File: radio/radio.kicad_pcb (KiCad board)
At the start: 2 copper layers, 63.5 x 63.5 mm, 6 parts, among them J1 CAS_stacking, U1 RFM69HCW

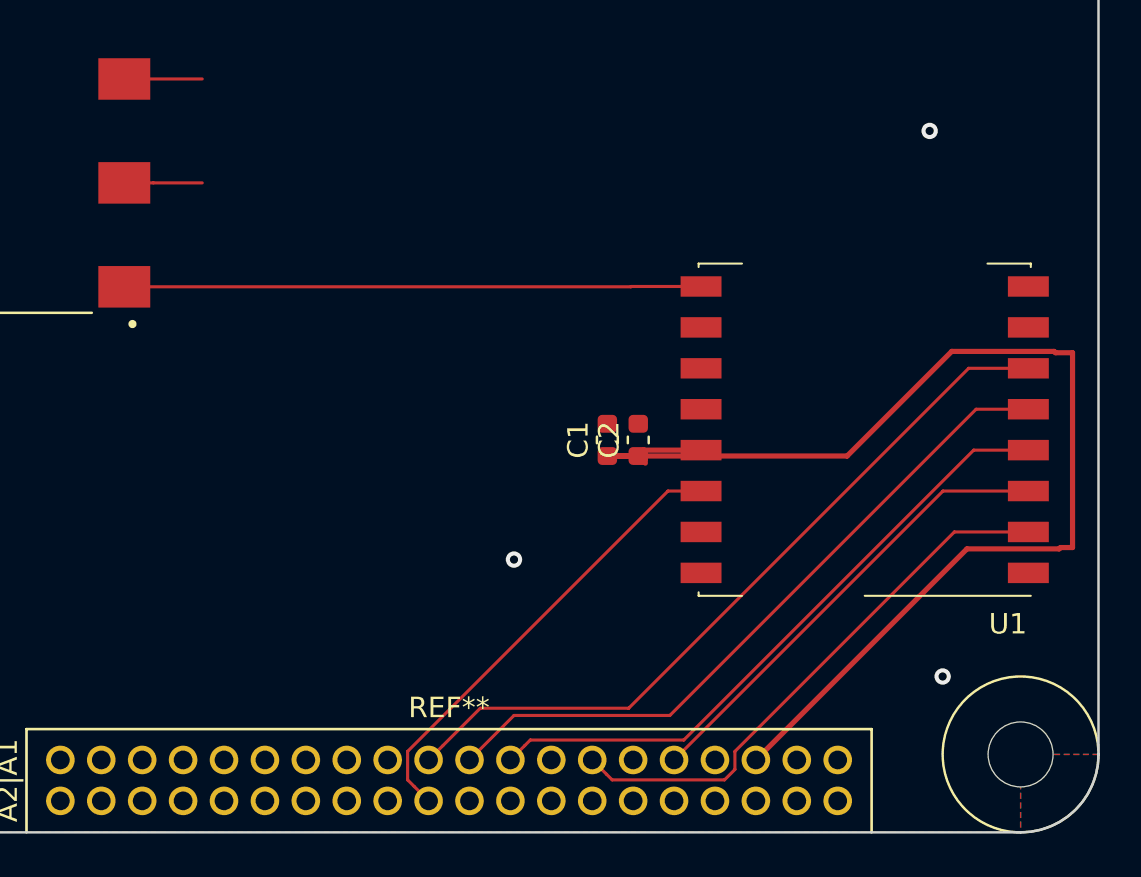
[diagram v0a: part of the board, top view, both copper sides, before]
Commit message: updated footprints
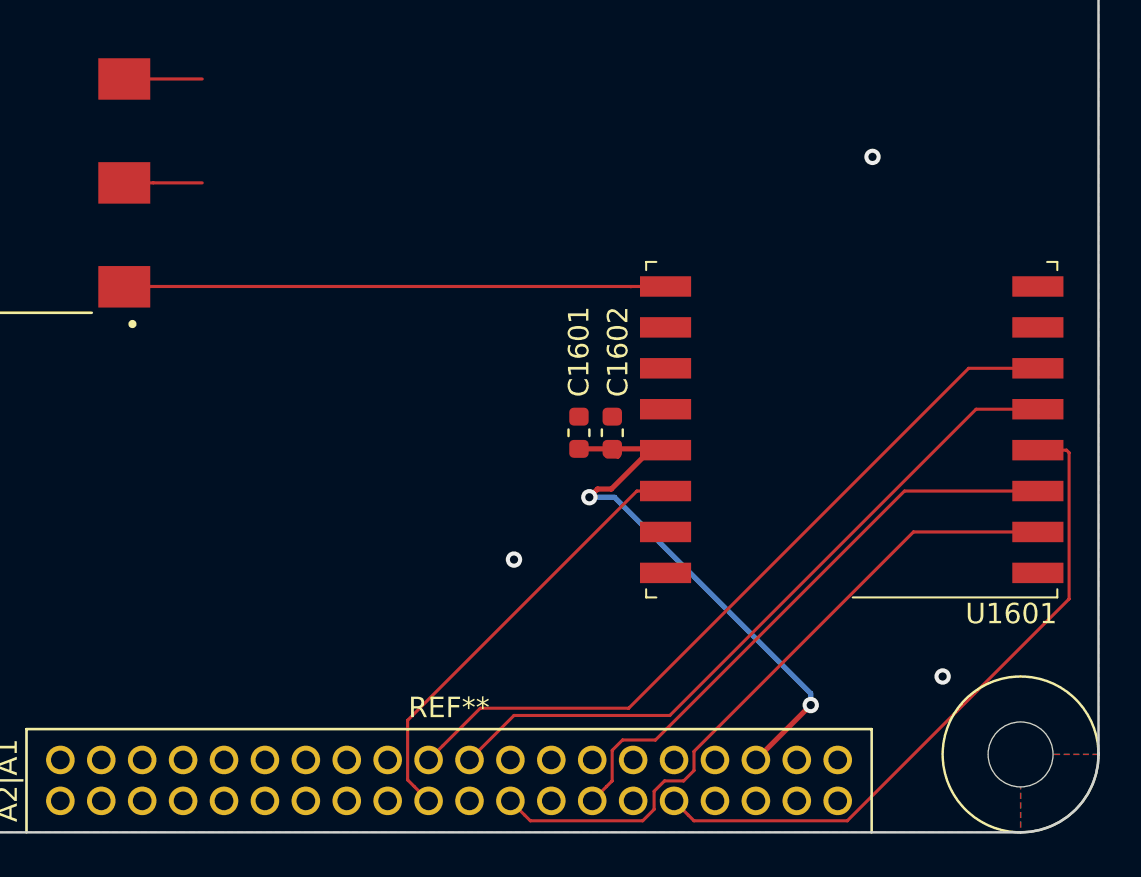
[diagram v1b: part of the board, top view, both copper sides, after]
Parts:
- removed C1: 10uF, Capacitor_SMD:C_0603_1608Metric
- removed C2: 0.1uF, Capacitor_SMD:C_0603_1608Metric
- removed G***: LOGO, star-common-lib:star
- removed J1: CAS_stacking, star-common-lib:CAS_physical
- removed U1: RFM69HCW, RF_Module:HOPERF_RFM9XW_SMD
- added C1601: 10uF, Capacitor_SMD:C_0603_1608Metric, F.Cu at (147.3, 92.9)
- added C1602: 0.1uF, Capacitor_SMD:C_0603_1608Metric, F.Cu at (149.0, 92.9)
- added J1001: CAS_stacking, star-common-lib:CAS_physical, F.Cu at (109.2, 112.4)
- added U1601: RFM69HCW, RF_Module:HOPERF_RFM69HW, F.Cu at (160.7, 92.7)
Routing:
- net +3V3: track 59.4 -> 29.1 mm, vias 0 -> 2
- net /SPI_MOSI: track 22.8 -> 28.9 mm
- net /SPI_MISO: track 27.3 -> 33.1 mm
- net /SPI_SCK: track 31.6 -> 33.7 mm
- net /ANT: track 28.2 -> 26.5 mm

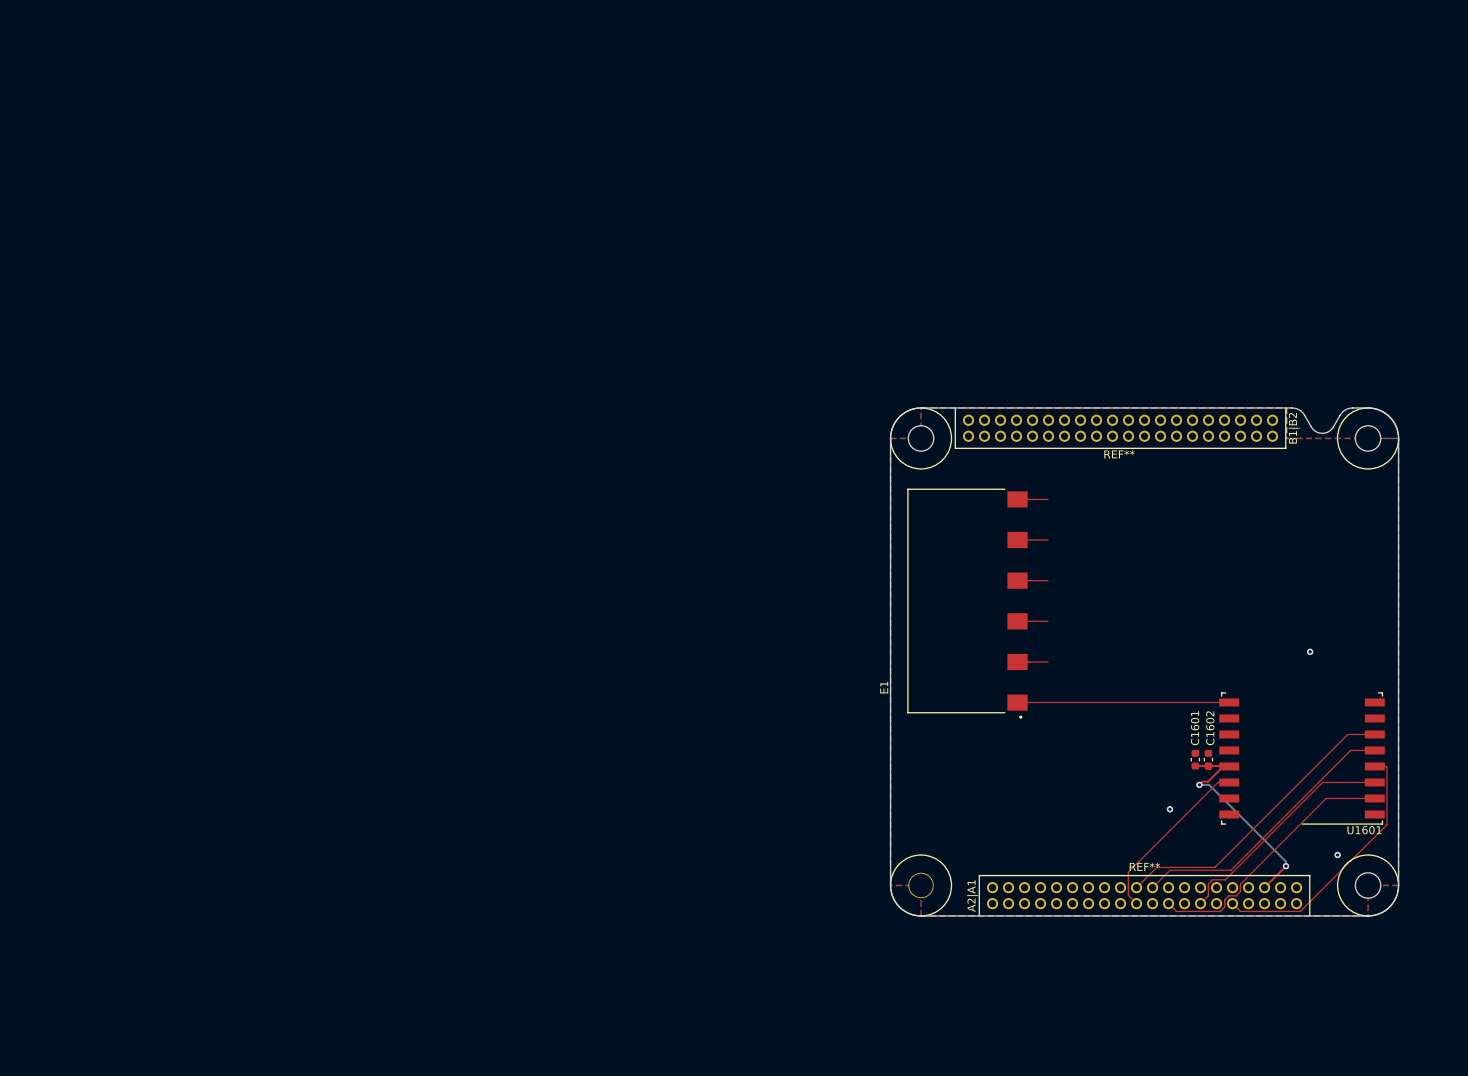
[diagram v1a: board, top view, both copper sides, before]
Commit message: 4-layer radio board
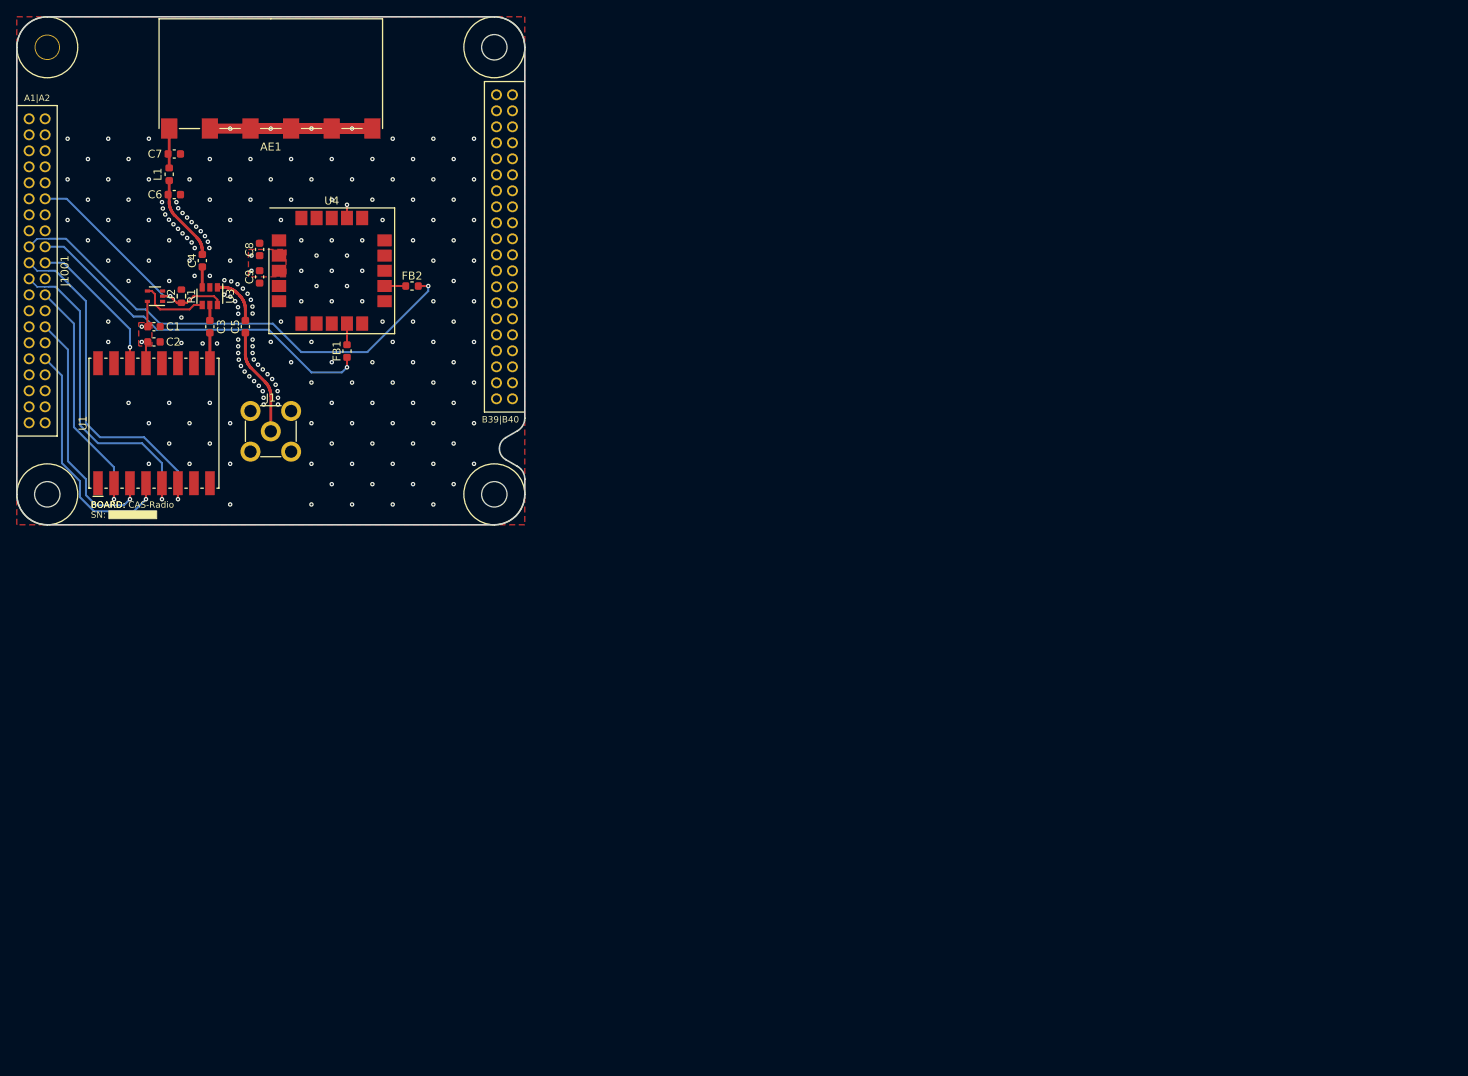
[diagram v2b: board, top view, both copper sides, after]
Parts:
- removed C1601: 10uF, Capacitor_SMD:C_0603_1608Metric
- removed C1602: 0.1uF, Capacitor_SMD:C_0603_1608Metric
- removed E1: ANT-433-SP, radio:XDCR_ANT-433-SP
- removed U1601: RFM69HCW, RF_Module:HOPERF_RFM69HW
- added AE1: ANT-433-SP, star-common-lib:ANT-433-SP, F.Cu at (31.8, 14.0)
- added C1: 10uF, Capacitor_SMD:C_0603_1608Metric, F.Cu at (17.1, 38.7)
- added C2: 0.1uF, Capacitor_SMD:C_0603_1608Metric, F.Cu at (17.1, 40.6)
- added C3: 1nF, Capacitor_SMD:C_0603_1608Metric, F.Cu at (24.1, 38.7)
- added C4: 1nF, Capacitor_SMD:C_0603_1608Metric, F.Cu at (23.2, 30.5)
- added C5: 1nF, Capacitor_SMD:C_0603_1608Metric, F.Cu at (28.6, 38.7)
- added C6: DNP, Capacitor_SMD:C_0603_1608Metric, F.Cu at (19.7, 22.2)
- added C7: DNP, Capacitor_SMD:C_0603_1608Metric, F.Cu at (19.7, 17.1)
- added C8: 1uF, Capacitor_SMD:C_0603_1608Metric, F.Cu at (30.4, 29.1)
- added C9: 0.1uF, Capacitor_SMD:C_0603_1608Metric, F.Cu at (30.4, 32.5)
- added FB1: Ferrite_Bead, Inductor_SMD:L_0603_1608Metric, F.Cu at (41.3, 41.8)
- added FB2: Ferrite_Bead, Inductor_SMD:L_0603_1608Metric, F.Cu at (49.4, 33.7)
- added J1: SMA, star-common-lib:SMA_Molex_73391-0083_Horizontal, F.Cu at (31.8, 51.8)
- added L1: 0R, Inductor_SMD:L_0603_1608Metric, F.Cu at (19.1, 19.7)
- added R1: 1k, Resistor_SMD:R_0603_1608Metric, F.Cu at (20.6, 34.9)
- added U1: RFM69HCW, star-common-lib:RFM69HCW-XXXS2, F.Cu at (17.1, 50.8)
- added U2: 74AHC1G04, Package_TO_SOT_SMD:SOT-353_SC-70-5, F.Cu at (17.3, 34.9)
- added U3: HMC544AE, Package_TO_SOT_SMD:SOT-23-6, F.Cu at (24.1, 34.9)
- added U4: ublox_SAM-M8Q, RF_GPS:ublox_SAM-M8Q, F.Cu at (39.4, 31.8)
- moved J1001 156.7 mm to (0.00, 0.00), turned to 0 degrees
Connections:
- J1001 pad A12: /CAS-bus/INT6 -> /A
- J1001 pad A17: /CAS-bus/I2C1_SCL -> /SCL
- J1001 pad A18: /CAS-bus/I2C1_SDA -> /SDA
- J1001 pad A19: /IO_38 -> /RF_RST
- J1001 pad A20: /IO_39 -> /RF_INT
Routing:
- net /SCL: track 0.00 -> 61.2 mm, vias 0 -> 1
- net /SDA: track 0.00 -> 45.7 mm, vias 0 -> 1
- net /RF_RST: track 0.00 -> 43.8 mm, vias 0 -> 1
- net +3V3: track 29.1 -> 68.7 mm, vias 2 -> 5
- net /IO_38: track 37.3 -> 0.00 mm
- net /A: track 0.00 -> 29.1 mm, vias 0 -> 1
- net /ANT: track 26.5 -> 3.80 mm
- net /IO_39: track 22.4 -> 0.00 mm
- net /RF_INT: track 0.00 -> 18.3 mm, vias 0 -> 1
- net GND: track 19.1 -> 36.8 mm, vias 3 -> 198
- net Net-(C5-Pad1): track 0.00 -> 13.4 mm
- net Net-(C4-Pad1): track 0.00 -> 10.9 mm
- net /B: track 0.00 -> 8.78 mm
- net /SPI_nSS1: track 34.4 -> 41.0 mm, vias 0 -> 1
- net Net-(C5-Pad2): track 0.00 -> 6.55 mm
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- added copper zone on F.Cu, net +3V3
- added copper zone on In1.Cu, net GND
- added copper zone on In2.Cu, net GND
- removed copper zone on B.Cu, net GND
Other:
- outline, holes or cut-outs redrawn
- copper layers 2 -> 4
- net class Default: clearance 0.2 -> 0.2032; trace_width 0.1524 -> 0.254; via_dia 0.8 -> 0.5588; via_drill 0.4 -> 0.254
- net class Microstrip added: clearance 0.2032, trace_width 0.379222, via_dia 0.5588, via_drill 0.254
- net class Power removed
- rule pad_to_mask_clearance: 0.051 -> 0
- rule trace_clearance: 0.2 -> 0.2032
- rule trace_min: 0.1524 -> 0.2032
- rule via_min_drill: 0.3 -> 0.254
- rule via_min_size: 0.4 -> 0.5588

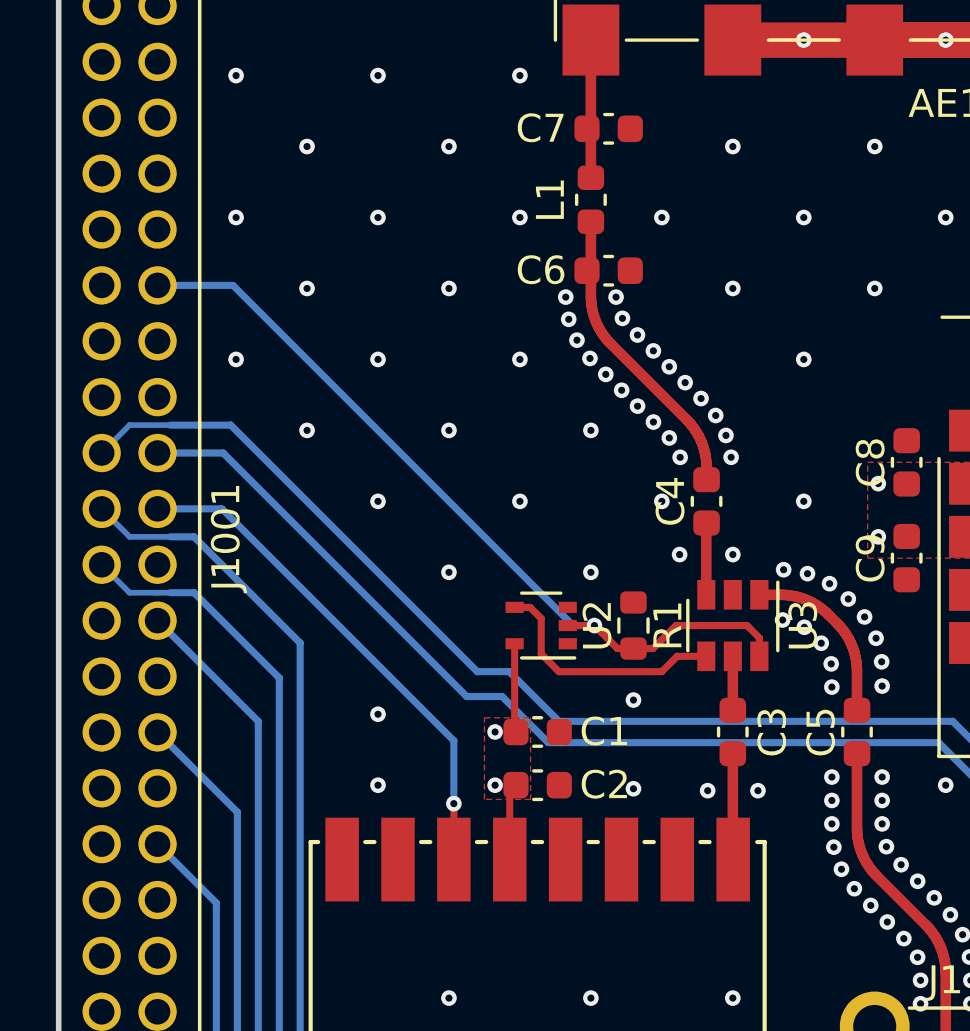
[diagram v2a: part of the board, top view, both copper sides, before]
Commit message: Added solder jumper to select source, removed radio INT
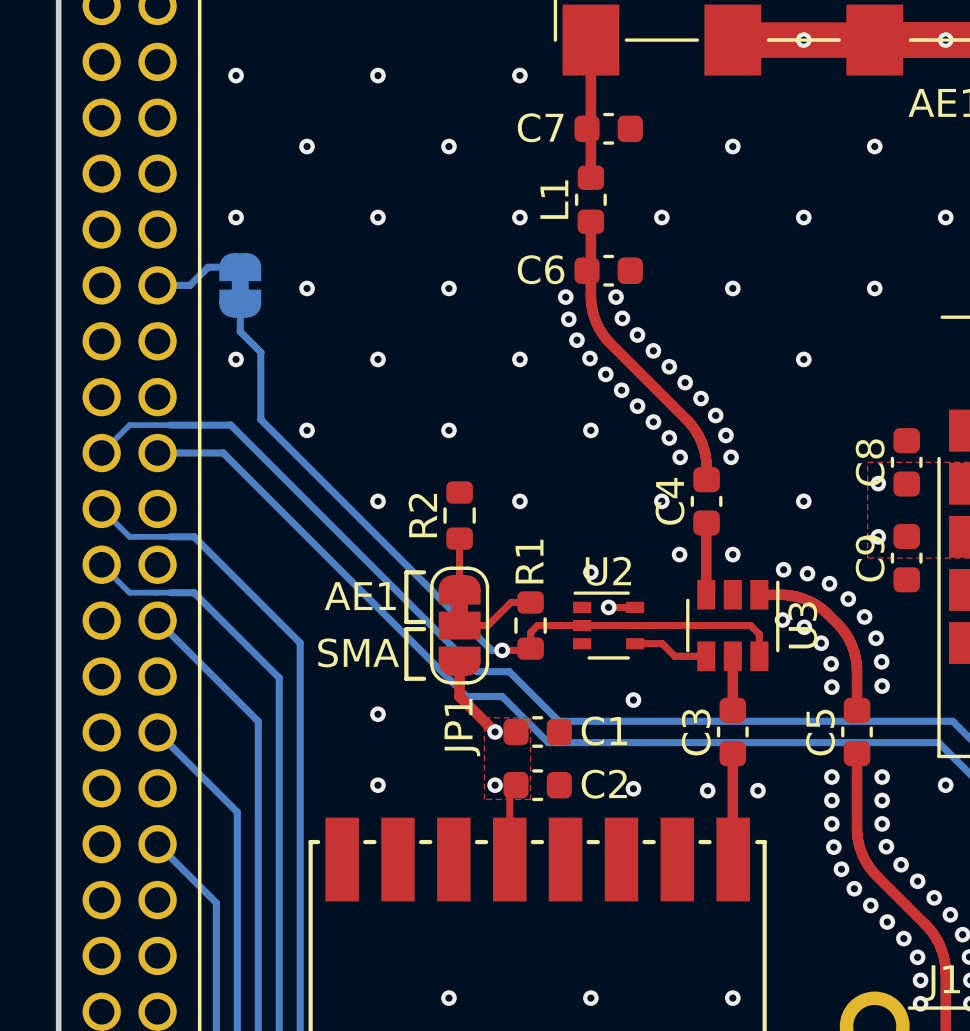
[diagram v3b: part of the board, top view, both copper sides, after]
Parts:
- added JP1: Default_Source, Jumper:SolderJumper-3_P1.3mm_Bridged12_RoundedPad1.0x1.5mm, F.Cu at (14.4, 34.9)
- added JP2: Jumper, Jumper:SolderJumper-2_P1.3mm_Bridged_RoundedPad1.0x1.5mm, B.Cu at (6.50, 22.8)
- added R2: 1k, Resistor_SMD:R_0603_1608Metric, F.Cu at (14.4, 31.0)
- moved R1 3.68 mm to (16.9, 34.9)
- moved U2 2.41 mm to (19.7, 34.9), turned to 0 degrees
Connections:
- J1001 pad A12: /A -> /RF_Source
- J1001 pad A20: /RF_INT -> /CAS-bus/INT8
- R1 pad 2: GND -> Net-(JP1-Pad2)
- U1 pad 14: /RF_INT -> Net-(U1-Pad14)
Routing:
- net /RF_INT: track 18.3 -> 0.00 mm, vias 1 -> 0
- net +3V3: track 68.7 -> 76.1 mm, vias 5 -> 6
- net /B: track 8.78 -> 2.73 mm
- net /RF_Source: track 0.00 -> 3.23 mm
- net Net-(JP1-Pad2): track 0.00 -> 2.88 mm
- net Net-(JP1-Pad1): track 0.00 -> 1.81 mm
- net /A: track 29.1 -> 27.3 mm
- net GND: vias 198 -> 197
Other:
- board text added: "AE1"
- board text added: "SMA"
